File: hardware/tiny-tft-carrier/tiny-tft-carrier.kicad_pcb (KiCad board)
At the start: 2 copper layers, 36.5 x 23 mm, 3 parts, among them J1 Questwise_TFT_042_96x54, U1 XIAO_ESP32_DIP14

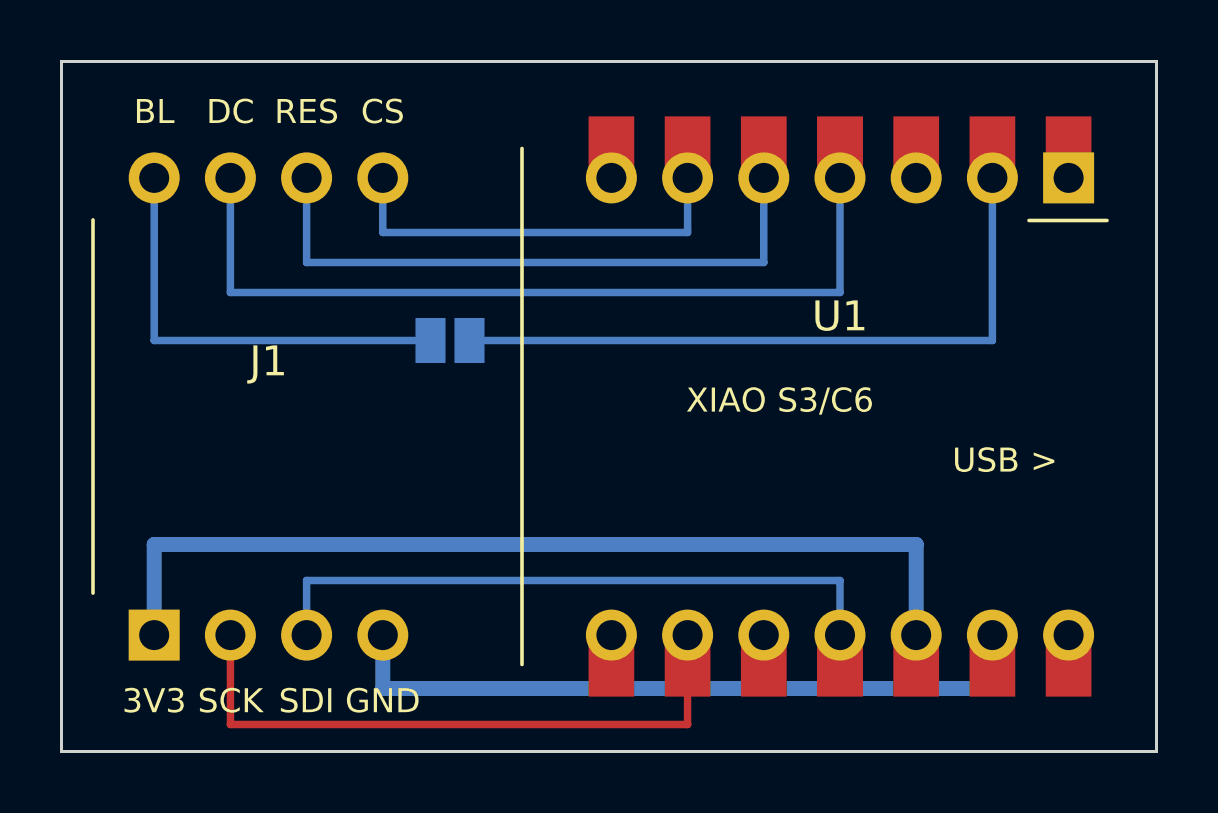
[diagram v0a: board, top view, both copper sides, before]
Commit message: Tiny TFT carrier: fix review findings and silkscreen overlaps
Silk: screen pin labels turned on end, XIAO labels on one row, back-side notes moved under the XIAO, jumper outline 0.24 mm clear of its pads, Fab value text hidden. Footprint properties carry their library ids with unique uuids. Sketch: seller registers sent with the screen off, XIAO ESP32-C3 pins added. DESIGN.md: plain S3 only (no Sense), antenna and USB-C overhang wording. Untrack the per-user .kicad_prl and ignore KiCad editor state. kicad-cli 10.0.7: ERC 0/0, DRC with parity 0 violations; Gerbers and drill re-exported.
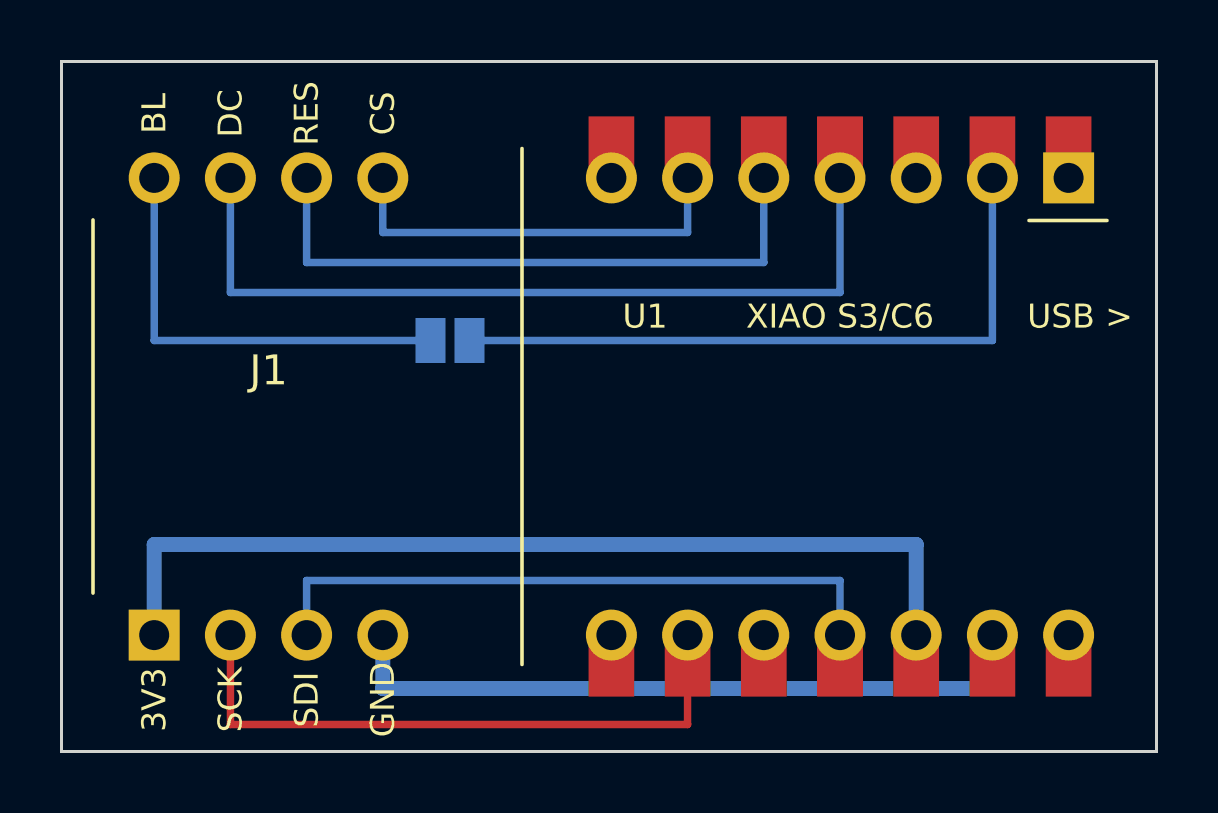
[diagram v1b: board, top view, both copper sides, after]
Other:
- board text added: "JP1 open: backlight on"
- board text removed: "JP1 open: backlight always on"
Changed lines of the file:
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@@
 	(descr "Seeed Studio XIAO (ESP32-S3 / ESP32-C6 / ESP32-C3), 2x7 2.54 mm, rows 15.24 mm, through holes plus edge pads for soldering flat")
 	(tags "XIAO ESP32")
-	(property "Reference" "U1" (at 0 -3 0) (layer "F.SilkS") (effects (font (size 1 1) (thickness 0.15))))
-	(property "Value" "XIAO_ESP32_DIP14" (at 0 3 0) (layer "F.Fab") (effects (font (size 1 1) (thickness 0.15))))
-	(property "Footprint" "" (at 0 0 0) (layer "F.Fab") (hide yes) (effects (font (size 1.27 1.27) (thickness 0.15))))
+	(property "Reference" "U1" (at -6.5 -3 0) (layer "F.SilkS") (effects (font (size 0.8 0.8) (thickness 0.12))))
+	(property "Value" "XIAO_ESP32_DIP14" (at 0 0 0) (layer "F.Fab") (hide yes) (effects (font (size 1 1) (thickness 0.15))))
+	(property "Footprint" "tiny-tft-carrier:XIAO_ESP32_DIP14" (at 0 0 0) (layer "F.Fab") (hide yes) (effects (font (size 1.27 1.27) (thickness 0.15))))
 	(property "Datasheet" "https://wiki.seeedstudio.com/xiao_esp32s3_getting_started/" (at 0 0 0) (layer "F.Fab") (hide yes) (effects (font (size 1.27 1.27) (thickness 0.15))))
 	(property "Description" "Seeed Studio XIAO ESP32-S3 / ESP32-C6, 14 edge pins" (at 0 0 0) (layer "F.Fab") (hide yes) (effects (font (size 1.27 1.27) (thickness 0.15))))
@@
 	(fp_rect (start -10.45 -8.9) (end 10.55 8.9) (stroke (width 0.1) (type solid)) (fill no) (layer "F.Fab"))
 	(fp_rect (start 10.55 -4.5) (end 12.05 4.5) (stroke (width 0.1) (type solid)) (fill no) (layer "F.Fab"))
-	(fp_text user "USB-C" (at 8 0 0) (layer "F.Fab") (effects (font (size 0.8 0.8) (thickness 0.12))))
+	(fp_text user "USB-C" (at 11.3 0 90) (layer "F.Fab") (effects (font (size 0.6 0.6) (thickness 0.1))))
 	(fp_rect (start -10.7 -10) (end 10.8 10) (stroke (width 0.05) (type solid)) (fill no) (layer "F.CrtYd"))
 	(fp_line (start -10.6 -8.6) (end -10.6 8.6) (stroke (width 0.12) (type solid)) (layer "F.SilkS"))
 	(fp_line (start 8.9 -6.2) (end 6.3 -6.2) (stroke (width 0.12) (type solid)) (layer "F.SilkS"))
-	(fp_text user "XIAO S3/C6" (at -2 -0.2 0) (layer "F.SilkS") (effects (font (size 0.8 0.8) (thickness 0.12))))
-	(fp_text user "USB >" (at 5.5 1.8 0) (layer "F.SilkS") (effects (font (size 0.8 0.8) (thickness 0.12))))
+	(fp_text user "XIAO S3/C6" (at 0 -3 0) (layer "F.SilkS") (effects (font (size 0.8 0.8) (thickness 0.12))))
+	(fp_text user "USB >" (at 8 -3 0) (layer "F.SilkS") (effects (font (size 0.8 0.8) (thickness 0.12))))
 	(pad "1" thru_hole rect (at 7.62 -7.62) (size 1.7 1.7) (drill 1) (layers "*.Cu" "*.Mask") (remove_unused_layers no) (net 11 "unconnected-(U1-D0-Pad1)"))
 	(pad "1" smd rect (at 7.62 -8.455) (size 1.524 2.432) (layers "F.Cu" "F.Mask") (net 11 "unconnected-(U1-D0-Pad1)"))
@@
 	(descr "Questwise 0.42 inch 96x54 TFT breakout, two rows of four pins. Row spacing and outline are photo estimates: measure before ordering")
 	(tags "TFT ST7735")
-	(property "Reference" "J1" (at 0 -1.5 0) (layer "F.SilkS") (effects (font (size 1 1) (thickness 0.15))))
-	(property "Value" "Questwise_TFT_042_96x54" (at 0 1.5 0) (layer "F.Fab") (effects (font (size 1 1) (thickness 0.15))))
-	(property "Footprint" "" (at 0 0 0) (layer "F.Fab") (hide yes) (effects (font (size 1.27 1.27) (thickness 0.15))))
+	(property "Reference" "J1" (at 0 -1.2 0) (layer "F.SilkS") (effects (font (size 1 1) (thickness 0.15))))
+	(property "Value" "Questwise_TFT_042_96x54" (at 0 0 0) (layer "F.Fab") (hide yes) (effects (font (size 1 1) (thickness 0.15))))
+	(property "Footprint" "tiny-tft-carrier:Questwise_TFT_042_96x54_2x4" (at 0 0 0) (layer "F.Fab") (hide yes) (effects (font (size 1.27 1.27) (thickness 0.15))))
 	(property "Datasheet" "https://www.tindie.com/products/questwise-ventures/miniature-042-rgb-color-tft-96x54-screen-display/" (at 0 0 0) (layer "F.Fab") (hide yes) (effects (font (size 1.27 1.27) (thickness 0.15))))
 	(property "Description" "0.42in 96x54 RGB TFT breakout, ST7735-family, SPI, 3.3 V only" (at 0 0 0) (layer "F.Fab") (hide yes) (effects (font (size 1.27 1.27) (thickness 0.15))))
 	(attr through_hole)
 	(fp_rect (start -6.45 -10.4) (end 6.45 10.4) (stroke (width 0.1) (type solid)) (fill no) (layer "F.Fab"))
-	(fp_text user "outline TO MEASURE" (at 0 4 0) (layer "F.Fab") (effects (font (size 0.8 0.8) (thickness 0.12))))
-	(fp_text user "flex cable end" (at -4.25 0 0) (layer "F.Fab") (effects (font (size 0.6 0.6) (thickness 0.1))))
+	(fp_text user "outline TO MEASURE" (at 0 1 0) (layer "F.Fab") (effects (font (size 0.6 0.6) (thickness 0.1))))
+	(fp_text user "< flex cable end" (at 0 2.4 0) (layer "F.Fab") (effects (font (size 0.6 0.6) (thickness 0.1))))
 	(fp_rect (start -6.7 -10.65) (end 6.7 10.65) (stroke (width 0.05) (type solid)) (fill no) (layer "F.CrtYd"))
-	(fp_text user "3V3" (at -3.81 9.82 0) (layer "F.SilkS") (effects (font (size 0.8 0.8) (thickness 0.12))))
-	(fp_text user "SCK" (at -1.27 9.82 0) (layer "F.SilkS") (effects (font (size 0.8 0.8) (thickness 0.12))))
-	(fp_text user "SDI" (at 1.27 9.82 0) (layer "F.SilkS") (effects (font (size 0.8 0.8) (thickness 0.12))))
-	(fp_text user "GND" (at 3.81 9.82 0) (layer "F.SilkS") (effects (font (size 0.8 0.8) (thickness 0.12))))
-	(fp_text user "BL" (at -3.81 -9.82 0) (layer "F.SilkS") (effects (font (size 0.8 0.8) (thickness 0.12))))
-	(fp_text user "DC" (at -1.27 -9.82 0) (layer "F.SilkS") (effects (font (size 0.8 0.8) (thickness 0.12))))
-	(fp_text user "RES" (at 1.27 -9.82 0) (layer "F.SilkS") (effects (font (size 0.8 0.8) (thickness 0.12))))
-	(fp_text user "CS" (at 3.81 -9.82 0) (layer "F.SilkS") (effects (font (size 0.8 0.8) (thickness 0.12))))
+	(fp_text user "3V3" (at -3.81 9.77 90) (layer "F.SilkS") (effects (font (size 0.8 0.8) (thickness 0.12))))
+	(fp_text user "SCK" (at -1.27 9.77 90) (layer "F.SilkS") (effects (font (size 0.8 0.8) (thickness 0.12))))
+	(fp_text user "SDI" (at 1.27 9.77 90) (layer "F.SilkS") (effects (font (size 0.8 0.8) (thickness 0.12))))
+	(fp_text user "GND" (at 3.81 9.77 90) (layer "F.SilkS") (effects (font (size 0.8 0.8) (thickness 0.12))))
+	(fp_text user "BL" (at -3.81 -9.77 90) (layer "F.SilkS") (effects (font (size 0.8 0.8) (thickness 0.12))))
+	(fp_text user "DC" (at -1.27 -9.77 90) (layer "F.SilkS") (effects (font (size 0.8 0.8) (thickness 0.12))))
+	(fp_text user "RES" (at 1.27 -9.77 90) (layer "F.SilkS") (effects (font (size 0.8 0.8) (thickness 0.12))))
+	(fp_text user "CS" (at 3.81 -9.77 90) (layer "F.SilkS") (effects (font (size 0.8 0.8) (thickness 0.12))))
 	(fp_line (start -5.85 -6.22) (end -5.85 6.22) (stroke (width 0.12) (type solid)) (layer "F.SilkS"))
 	(pad "1" thru_hole rect (at -3.81 7.62) (size 1.7 1.7) (drill 1) (layers "*.Cu" "*.Mask") (remove_unused_layers no) (net 1 "+3V3"))
@@
 	(descr "Two-pad solder jumper, open by default, 1.0 x 1.5 mm pads, 0.3 mm gap")
 	(tags "solder jumper open")
-	(property "Reference" "JP1" (at 0 1.7 0) (layer "B.SilkS") (effects (font (size 0.8 0.8) (thickness 0.12)) (justify mirror)))
-	(property "Value" "SolderJumper_2_Open" (at 0 -1.9 0) (layer "B.Fab") (effects (font (size 1 1) (thickness 0.15)) (justify mirror)))
-	(property "Footprint" "" (at 0 0 0) (layer "B.Fab") (hide yes) (effects (font (size 1.27 1.27) (thickness 0.15)) (justify mirror)))
+	(property "Reference" "JP1" (at 0 2 0) (layer "B.SilkS") (effects (font (size 0.8 0.8) (thickness 0.12)) (justify mirror)))
+	(property "Value" "SolderJumper_2_Open" (at 0 0 0) (layer "B.Fab") (hide yes) (effects (font (size 1 1) (thickness 0.15)) (justify mirror)))
+	(property "Footprint" "tiny-tft-carrier:SolderJumper_2_Open" (at 0 0 0) (layer "B.Fab") (hide yes) (effects (font (size 1.27 1.27) (thickness 0.15)) (justify mirror)))
 	(property "Datasheet" "" (at 0 0 0) (layer "B.Fab") (hide yes) (effects (font (size 1.27 1.27) (thickness 0.15)) (justify mirror)))
 	(property "Description" "Solder jumper, open by default" (at 0 0 0) (layer "B.Fab") (hide yes) (effects (font (size 1.27 1.27) (thickness 0.15)) (justify mirror)))
 	(attr smd exclude_from_pos_files exclude_from_bom)
-	(fp_rect (start -1.4 -1) (end 1.4 1) (stroke (width 0.05) (type solid)) (fill no) (layer "B.CrtYd"))
-	(fp_line (start -1.4 -0.95) (end 1.4 -0.95) (stroke (width 0.12) (type solid)) (layer "B.SilkS"))
-	(fp_line (start -1.4 0.95) (end 1.4 0.95) (stroke (width 0.12) (type solid)) (layer "B.SilkS"))
+	(fp_rect (start -1.4 -1.25) (end 1.4 1.25) (stroke (width 0.05) (type solid)) (fill no) (layer "B.CrtYd"))
+	(fp_line (start -1.4 -1.05) (end 1.4 -1.05) (stroke (width 0.12) (type solid)) (layer "B.SilkS"))
+	(fp_line (start -1.4 1.05) (end 1.4 1.05) (stroke (width 0.12) (type solid)) (layer "B.SilkS"))
 	(pad "1" smd rect (at -0.65 0) (size 1 1.5) (layers "B.Cu" "B.Mask") (net 8 "BL"))
 	(pad "2" smd rect (at 0.65 0) (size 1 1.5) (layers "B.Cu" "B.Mask") (net 9 "BL_D1"))
 )
 	(gr_rect (start 94.05 88.5) (end 130.55 111.5) (stroke (width 0.1) (type default)) (fill no) (layer "Edge.Cuts"))
-	(gr_text "Tiny TFT carrier rev A" (at 103 89.6 0) (layer "B.SilkS") (effects (font (size 0.8 0.8) (thickness 0.12)) (justify mirror)))
-	(gr_text "JP1 bridged: D1 drives BL" (at 108 100.6 0) (layer "B.SilkS") (effects (font (size 0.8 0.8) (thickness 0.12)) (justify mirror)))
-	(gr_text "JP1 open: backlight always on" (at 108 102 0) (layer "B.SilkS") (effects (font (size 0.8 0.8) (thickness 0.12)) (justify mirror)))
+	(gr_text "Tiny TFT carrier rev A" (at 119 100.6 0) (layer "B.SilkS") (effects (font (size 0.8 0.8) (thickness 0.12)) (justify mirror)))
+	(gr_text "JP1 bridged: D1 drives BL" (at 119 102 0) (layer "B.SilkS") (effects (font (size 0.8 0.8) (thickness 0.12)) (justify mirror)))
+	(gr_text "JP1 open: backlight on" (at 119 103.4 0) (layer "B.SilkS") (effects (font (size 0.8 0.8) (thickness 0.12)) (justify mirror)))
 	(segment (start 120 107.62) (end 120 105.8) (width 0.25) (layer "B.Cu") (net 4))
 	(segment (start 120 105.8) (end 102.22 105.8) (width 0.25) (layer "B.Cu") (net 4))
